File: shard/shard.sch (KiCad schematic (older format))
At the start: 2 parts, among them J0 Shard

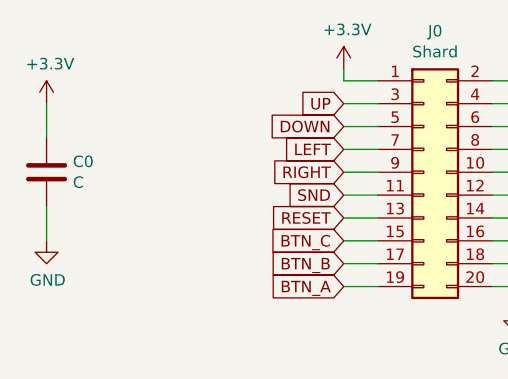
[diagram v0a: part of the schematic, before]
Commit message: added capacitor value
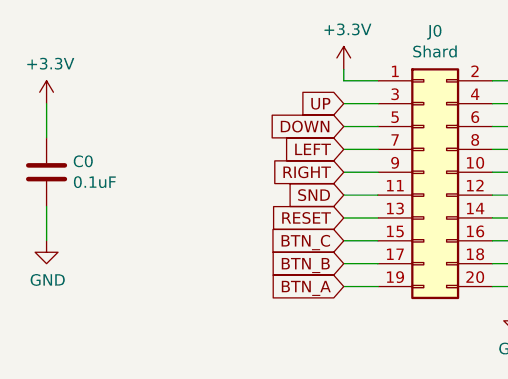
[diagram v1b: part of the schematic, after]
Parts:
- C0: value C -> 0.1uF
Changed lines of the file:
@@
 P 4450 3200
 F 0 "C0" H 4565 3246 50  0000 L CNN
-F 1 "C" H 4565 3155 50  0000 L CNN
+F 1 "0.1uF" H 4565 3155 50  0000 L CNN
 F 2 "Capacitor_THT:C_Rect_L7.0mm_W2.5mm_P5.00mm" H 4488 3050 50  0001 C CNN
 F 3 "~" H 4450 3200 50  0001 C CNN

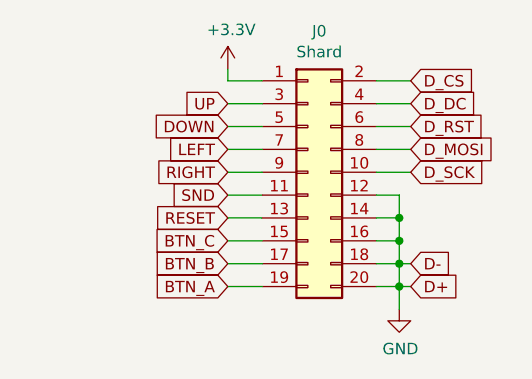
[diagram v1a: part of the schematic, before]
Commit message: disconnected D- & D+ to fix GND net
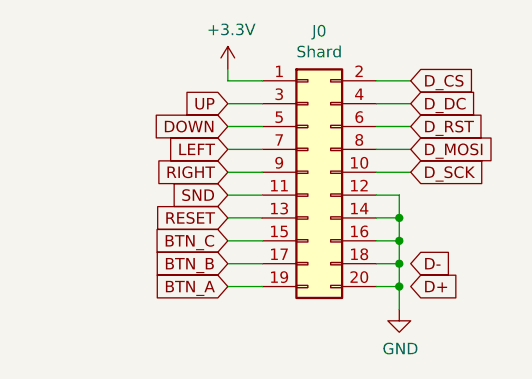
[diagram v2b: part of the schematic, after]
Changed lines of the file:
@@
 Text GLabel 6550 3600 2    50   Input ~ 0
 D-
-Wire Wire Line
-	6500 3600 6550 3600
-Wire Wire Line
-	6500 3700 6550 3700
 $EndSCHEMATC

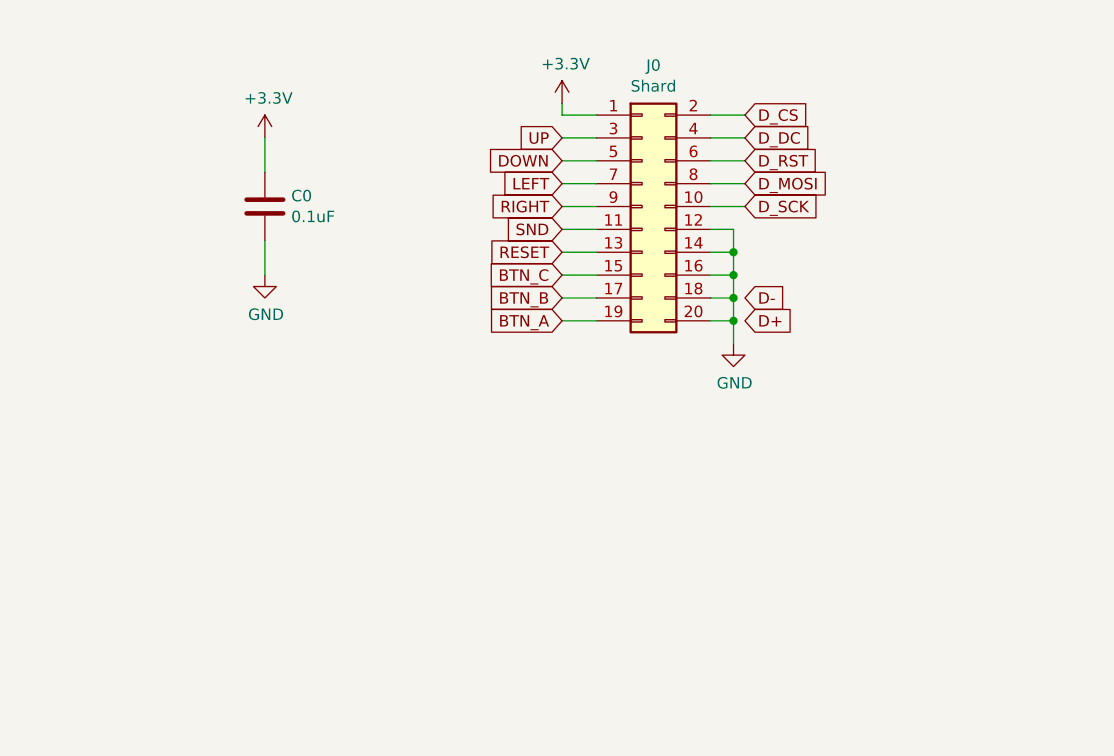
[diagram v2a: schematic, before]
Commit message: Template updated to edge connector
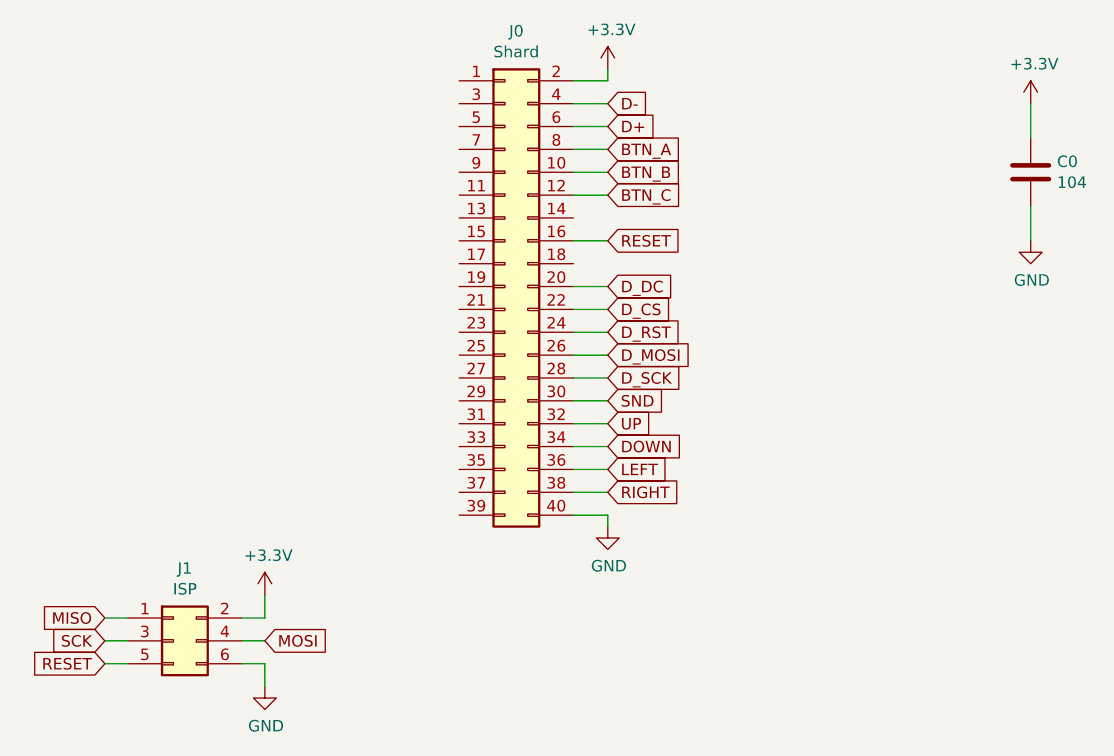
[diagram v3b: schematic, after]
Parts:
- removed J0: Shard, Connector_PinHeader_2.54mm:PinHeader_2x10_P2.54mm_Vertical, symbol Connector_Generic:Conn_02x10_Odd_Even
- added J0: Shard, Custom Footprints:Samtec_MEC8-120-02-L-D-RA1_Edge, symbol Connector_Generic:Conn_02x20_Odd_Even
- added J1: ISP, Connector_PinHeader_2.54mm:PinHeader_2x03_P2.54mm_Vertical, symbol Connector_Generic:Conn_02x03_Odd_Even
- C0: value 0.1uF -> 104
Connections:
- net +3V3: now also J0.2 (Pin_2), J1.2 (Pin_2)
- net BTN_A: now also J0.8 (Pin_8)
- net BTN_B: now also J0.10 (Pin_10)
- net BTN_C: now also J0.12 (Pin_12)
- net D+: now also J0.6 (Pin_6)
- net D-: now also J0.4 (Pin_4)
- net DOWN: now also J0.34 (Pin_34)
- net D_CS: now also J0.22 (Pin_22)
- net D_DC: now also J0.20 (Pin_20)
- net D_MOSI: now also J0.26 (Pin_26)
- net D_RST: now also J0.24 (Pin_24)
- net D_SCK: now also J0.28 (Pin_28)
- net GND: now also J0.40 (Pin_40), J1.6 (Pin_6)
- net LEFT: now also J0.36 (Pin_36)
- net RESET: now also J0.16 (Pin_16), J1.5 (Pin_5)
- net RIGHT: now also J0.38 (Pin_38)
- net SND: now also J0.30 (Pin_30)
- net UP: now also J0.32 (Pin_32)
- new net MISO: J1.1 (Pin_1)
- new net MOSI: J1.4 (Pin_4)
- new net SCK: J1.3 (Pin_3)
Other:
- moved on the sheet: C0
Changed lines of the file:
@@
 $EndDescr
-$Comp
-L Connector_Generic:Conn_02x10_Odd_Even J0
-U 1 1 5BE693B2
-P 6100 3200
-F 0 "J0" H 6150 3817 50  0000 C CNN
-F 1 "Shard" H 6150 3726 50  0000 C CNN
-F 2 "Connector_PinHeader_2.54mm:PinHeader_2x10_P2.54mm_Vertical" H 6100 3200 50  0001 C CNN
-F 3 "~" H 6100 3200 50  0001 C CNN
-	1    6100 3200
-	1    0    0    -1
-$EndComp
 $Comp
 L Device:C C0
 U 1 1 5BE6947B
-P 4450 3200
-F 0 "C0" H 4565 3246 50  0000 L CNN
-F 1 "0.1uF" H 4565 3155 50  0000 L CNN
-F 2 "Capacitor_THT:C_Rect_L7.0mm_W2.5mm_P5.00mm" H 4488 3050 50  0001 C CNN
-F 3 "~" H 4450 3200 50  0001 C CNN
-	1    4450 3200
+P 7800 3050
+F 0 "C0" H 7915 3096 50  0000 L CNN
+F 1 "104" H 7915 3005 50  0000 L CNN
+F 2 "Capacitor_THT:C_Rect_L7.0mm_W2.5mm_P5.00mm" H 7838 2900 50  0001 C CNN
+F 3 "~" H 7800 3050 50  0001 C CNN
+	1    7800 3050
 	1    0    0    -1
 $EndComp
@@
 L power:+3.3V #PWR0101
 U 1 1 5BE699E5
-P 5750 2750
-F 0 "#PWR0101" H 5750 2600 50  0001 C CNN
-F 1 "+3.3V" H 5765 2923 50  0000 C CNN
-F 2 "" H 5750 2750 50  0001 C CNN
-F 3 "" H 5750 2750 50  0001 C CNN
-	1    5750 2750
-	1    0    0    -1
-$EndComp
-$Comp
-L power:GND #PWR0102
-U 1 1 5BE69B29
-P 6500 3800
-F 0 "#PWR0102" H 6500 3550 50  0001 C CNN
-F 1 "GND" H 6505 3627 50  0000 C CNN
-F 2 "" H 6500 3800 50  0001 C CNN
-F 3 "" H 6500 3800 50  0001 C CNN
-	1    6500 3800
+P 5950 2600
+F 0 "#PWR0101" H 5950 2450 50  0001 C CNN
+F 1 "+3.3V" H 5965 2773 50  0000 C CNN
+F 2 "" H 5950 2600 50  0001 C CNN
+F 3 "" H 5950 2600 50  0001 C CNN
+	1    5950 2600
 	1    0    0    -1
 $EndComp
@@
 L power:GND #PWR0103
 U 1 1 5BE69CAB
-P 4450 3500
-F 0 "#PWR0103" H 4450 3250 50  0001 C CNN
-F 1 "GND" H 4455 3327 50  0000 C CNN
-F 2 "" H 4450 3500 50  0001 C CNN
-F 3 "" H 4450 3500 50  0001 C CNN
-	1    4450 3500
-	1    0    0    -1
-$EndComp
-Wire Wire Line
-	6400 3700 6500 3700
-Wire Wire Line
-	6500 3700 6500 3800
-Wire Wire Line
-	6400 3600 6500 3600
-Wire Wire Line
-	6500 3600 6500 3700
-Connection ~ 6500 3700
-Wire Wire Line
-	6400 3500 6500 3500
-Wire Wire Line
-	6500 3500 6500 3600
-Connection ~ 6500 3600
-Wire Wire Line
-	6400 3400 6500 3400
-Wire Wire Line
-	6500 3400 6500 3500
-Connection ~ 6500 3500
-Wire Wire Line
-	6400 3300 6500 3300
-Wire Wire Line
-	6500 3300 6500 3400
-Connection ~ 6500 3400
-Wire Wire Line
-	5750 2750 5750 2800
-Wire Wire Line
-	5750 2800 5900 2800
-Text GLabel 6550 2800 2    50   Input ~ 0
+P 7800 3350
+F 0 "#PWR0103" H 7800 3100 50  0001 C CNN
+F 1 "GND" H 7805 3177 50  0000 C CNN
+F 2 "" H 7800 3350 50  0001 C CNN
+F 3 "" H 7800 3350 50  0001 C CNN
+	1    7800 3350
+	1    0    0    -1
+$EndComp
+Text GLabel 5950 3650 2    50   Input ~ 0
 D_CS
-Text GLabel 6550 2900 2    50   Input ~ 0
+Text GLabel 5950 3550 2    50   Input ~ 0
 D_DC
-Text GLabel 6550 3000 2    50   Input ~ 0
+Text GLabel 5950 3750 2    50   Input ~ 0
 D_RST
-Text GLabel 6550 3100 2    50   Input ~ 0
+Text GLabel 5950 3850 2    50   Input ~ 0
 D_MOSI
-Text GLabel 6550 3200 2    50   Input ~ 0
+Text GLabel 5950 3950 2    50   Input ~ 0
 D_SCK
-Wire Wire Line
-	6400 2800 6550 2800
-Wire Wire Line
-	6400 2900 6550 2900
-Wire Wire Line
-	6400 3000 6550 3000
-Wire Wire Line
-	6400 3100 6550 3100
-Wire Wire Line
-	6400 3200 6550 3200
-Text GLabel 5750 2900 0    50   Input ~ 0
+Text GLabel 5950 4150 2    50   Input ~ 0
 UP
-Text GLabel 5750 3000 0    50   Input ~ 0
+Text GLabel 5950 4250 2    50   Input ~ 0
 DOWN
-Text GLabel 5750 3100 0    50   Input ~ 0
+Text GLabel 5950 4350 2    50   Input ~ 0
 LEFT
-Text GLabel 5750 3200 0    50   Input ~ 0
+Text GLabel 5950 4450 2    50   Input ~ 0
 RIGHT
-Text GLabel 5750 3300 0    50   Input ~ 0
+Text GLabel 5950 4050 2    50   Input ~ 0
 SND
-Text GLabel 5750 3400 0    50   Input ~ 0
+Text GLabel 5950 3350 2    50   Input ~ 0
 RESET
-Text GLabel 5750 3500 0    50   Input ~ 0
+Text GLabel 5950 3150 2    50   Input ~ 0
 BTN_C
-Text GLabel 5750 3600 0    50   Input ~ 0
+Text GLabel 5950 3050 2    50   Input ~ 0
 BTN_B
-Text GLabel 5750 3700 0    50   Input ~ 0
+Text GLabel 5950 2950 2    50   Input ~ 0
 BTN_A
-Wire Wire Line
-	5750 2900 5900 2900
-Wire Wire Line
-	5750 3000 5900 3000
-Wire Wire Line
-	5750 3100 5900 3100
-Wire Wire Line
-	5750 3200 5900 3200
-Wire Wire Line
-	5750 3300 5900 3300
-Wire Wire Line
-	5750 3400 5900 3400
-Wire Wire Line
-	5750 3500 5900 3500
-Wire Wire Line
-	5750 3600 5900 3600
-Wire Wire Line
-	5750 3700 5900 3700
 $Comp
 L power:+3.3V #PWR0104
 U 1 1 5BE80463
-P 4450 2900
-F 0 "#PWR0104" H 4450 2750 50  0001 C CNN
-F 1 "+3.3V" H 4465 3073 50  0000 C CNN
-F 2 "" H 4450 2900 50  0001 C CNN
-F 3 "" H 4450 2900 50  0001 C CNN
-	1    4450 2900
-	1    0    0    -1
-$EndComp
-Wire Wire Line
-	4450 2900 4450 3050
-Wire Wire Line
-	4450 3350 4450 3500
-Text GLabel 6550 3700 2    50   Input ~ 0
+P 7800 2750
+F 0 "#PWR0104" H 7800 2600 50  0001 C CNN
+F 1 "+3.3V" H 7815 2923 50  0000 C CNN
+F 2 "" H 7800 2750 50  0001 C CNN
+F 3 "" H 7800 2750 50  0001 C CNN
+	1    7800 2750
+	1    0    0    -1
+$EndComp
+Wire Wire Line
+	7800 2750 7800 2900
+Wire Wire Line
+	7800 3200 7800 3350
+Text GLabel 5950 2850 2    50   Input ~ 0
 D+
-Text GLabel 6550 3600 2    50   Input ~ 0
+Text GLabel 5950 2750 2    50   Input ~ 0
 D-
+$Comp
+L Connector_Generic:Conn_02x03_Odd_Even J1
+U 1 1 5BE8415C
+P 4050 5100
+F 0 "J1" H 4100 5417 50  0000 C CNN
+F 1 "ISP" H 4100 5326 50  0000 C CNN
+F 2 "Connector_PinHeader_2.54mm:PinHeader_2x03_P2.54mm_Vertical" H 4050 5100 50  0001 C CNN
+F 3 "~" H 4050 5100 50  0001 C CNN
+	1    4050 5100
+	1    0    0    -1
+$EndComp
+Text GLabel 3750 5000 0    50   Input ~ 0
+MISO
+Text GLabel 3750 5100 0    50   Input ~ 0
+SCK
+Text GLabel 3750 5200 0    50   Input ~ 0
+RESET
+$Comp
+L power:GND #PWR0107
+U 1 1 5BE8517E
+P 4450 5300
+F 0 "#PWR0107" H 4450 5050 50  0001 C CNN
+F 1 "GND" H 4455 5127 50  0000 C CNN
+F 2 "" H 4450 5300 50  0001 C CNN
+F 3 "" H 4450 5300 50  0001 C CNN
+	1    4450 5300
+	1    0    0    -1
+$EndComp
+$Comp
+L power:+3.3V #PWR0108
+U 1 1 5BE8525D
+P 4450 4900
+F 0 "#PWR0108" H 4450 4750 50  0001 C CNN
+F 1 "+3.3V" H 4465 5073 50  0000 C CNN
+F 2 "" H 4450 4900 50  0001 C CNN
+F 3 "" H 4450 4900 50  0001 C CNN
+	1    4450 4900
+	1    0    0    -1
+$EndComp
+Text GLabel 4450 5100 2    50   Input ~ 0
+MOSI
+Wire Wire Line
+	3750 5000 3850 5000
+Wire Wire Line
+	3750 5100 3850 5100
+Wire Wire Line
+	3750 5200 3850 5200
+Wire Wire Line
+	4450 4900 4450 5000
+Wire Wire Line
+	4450 5000 4350 5000
+Wire Wire Line
+	4350 5100 4450 5100
+Wire Wire Line
+	4450 5300 4450 5200
+Wire Wire Line
+	4450 5200 4350 5200
+$Comp
+L power:GND #PWR0102
+U 1 1 5BE9B3E3
+P 5950 4600
+F 0 "#PWR0102" H 5950 4350 50  0001 C CNN
+F 1 "GND" H 5955 4427 50  0000 C CNN
+F 2 "" H 5950 4600 50  0001 C CNN
+F 3 "" H 5950 4600 50  0001 C CNN
+	1    5950 4600
+	1    0    0    -1
+$EndComp
+$Comp
+L Connector_Generic:Conn_02x20_Odd_Even J0
+U 1 1 5BF0E178
+P 5500 3550
+F 0 "J0" H 5550 4667 50  0000 C CNN
+F 1 "Shard" H 5550 4576 50  0000 C CNN
+F 2 "Custom Footprints:Samtec_MEC8-120-02-L-D-RA1_Edge" H 5500 3550 50  0001 C CNN
+F 3 "~" H 5500 3550 50  0001 C CNN
+	1    5500 3550
+	1    0    0    -1
+$EndComp
+Wire Wire Line
+	5800 4550 5950 4550
+Wire Wire Line
+	5950 4550 5950 4600
+Wire Wire Line
+	5800 2950 5950 2950
+Wire Wire Line
+	5800 3050 5950 3050
+Wire Wire Line
+	5800 3150 5950 3150
+Wire Wire Line
+	5800 3350 5950 3350
+Wire Wire Line
+	5800 3550 5950 3550
+Wire Wire Line
+	5800 3750 5950 3750
+Wire Wire Line
+	5800 3850 5950 3850
+Wire Wire Line
+	5800 3950 5950 3950
+Wire Wire Line
+	5800 4050 5950 4050
+Wire Wire Line
+	5800 4150 5950 4150
+Wire Wire Line
+	5800 4250 5950 4250
+Wire Wire Line
+	5800 4350 5950 4350
+Wire Wire Line
+	5800 4450 5950 4450
+Wire Wire Line
+	5800 2650 5950 2650
+Wire Wire Line
+	5950 2650 5950 2600
+Wire Wire Line
+	5800 2750 5950 2750
+Wire Wire Line
+	5800 2850 5950 2850
+Wire Wire Line
+	5800 3650 5950 3650
 $EndSCHEMATC

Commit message: ::eyeroll::
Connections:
- net D_CS: now also J0.20 (Pin_20); no longer J0.22 (Pin_22)
- net D_DC: now also J0.22 (Pin_22); no longer J0.20 (Pin_20)
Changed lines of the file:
@@
 	1    0    0    -1
 $EndComp
+Text GLabel 5950 3550 2    50   Input ~ 0
+D_CS
 Text GLabel 5950 3650 2    50   Input ~ 0
-D_CS
-Text GLabel 5950 3550 2    50   Input ~ 0
 D_DC
 Text GLabel 5950 3750 2    50   Input ~ 0
